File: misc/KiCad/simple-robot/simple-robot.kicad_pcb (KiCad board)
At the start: 4 copper layers, 100 x 100 mm, 69 parts, among them J1 MotLA, J10 Screw_Terminal_2_P5.00mm, J11 JSTHCSR04, J12 IR_RF, J13 IR_LF, J14 GV, J15 JST RF-LOG, J16 RF_PWR, J2 MotLB, J3 Servo, J4 MotRA, J5 MotRB, J6 ENC_LF, J7 ENC_LR, J8 ENC_RF, J9 ENC_RR, P1 Port Expander, SW1 RotaryEncoder_Switch, U1 Pico2, U2 CD4049UB

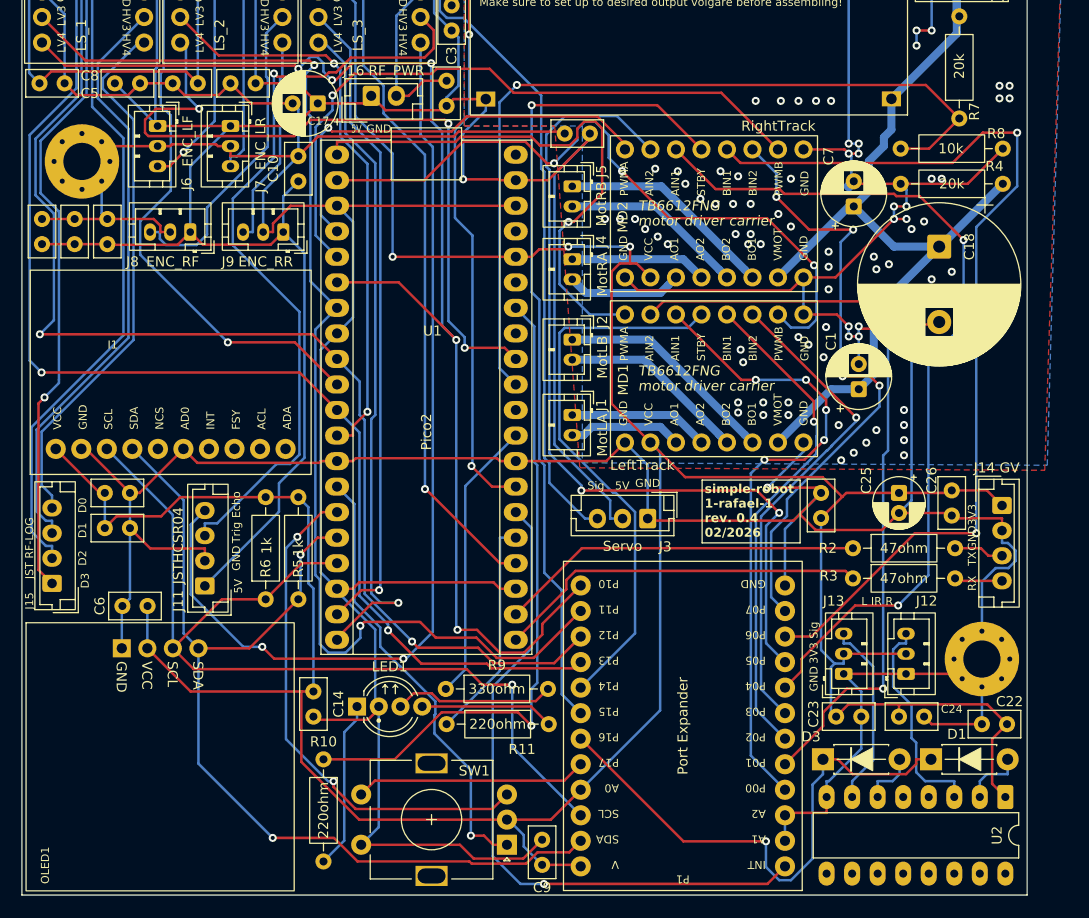
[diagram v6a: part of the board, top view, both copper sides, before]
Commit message: rp235x E9 erratum hitting: rotary encoder should be reffed to common GND instead of 3V3
Pulldowns on RP235x only work on after stepping A4, all my boards are
stepping A2. So thereference for the encoder should not be 3V3 because
that we will need to pull down and that will latch on the RP.

Workaround is to add pulldowns which i will do for now but a proper
workaround is to change the pcb and schematic to have a common GND
instead of common 3V3 on the encoder and use pullup.

This commit changes schematic and pcb.
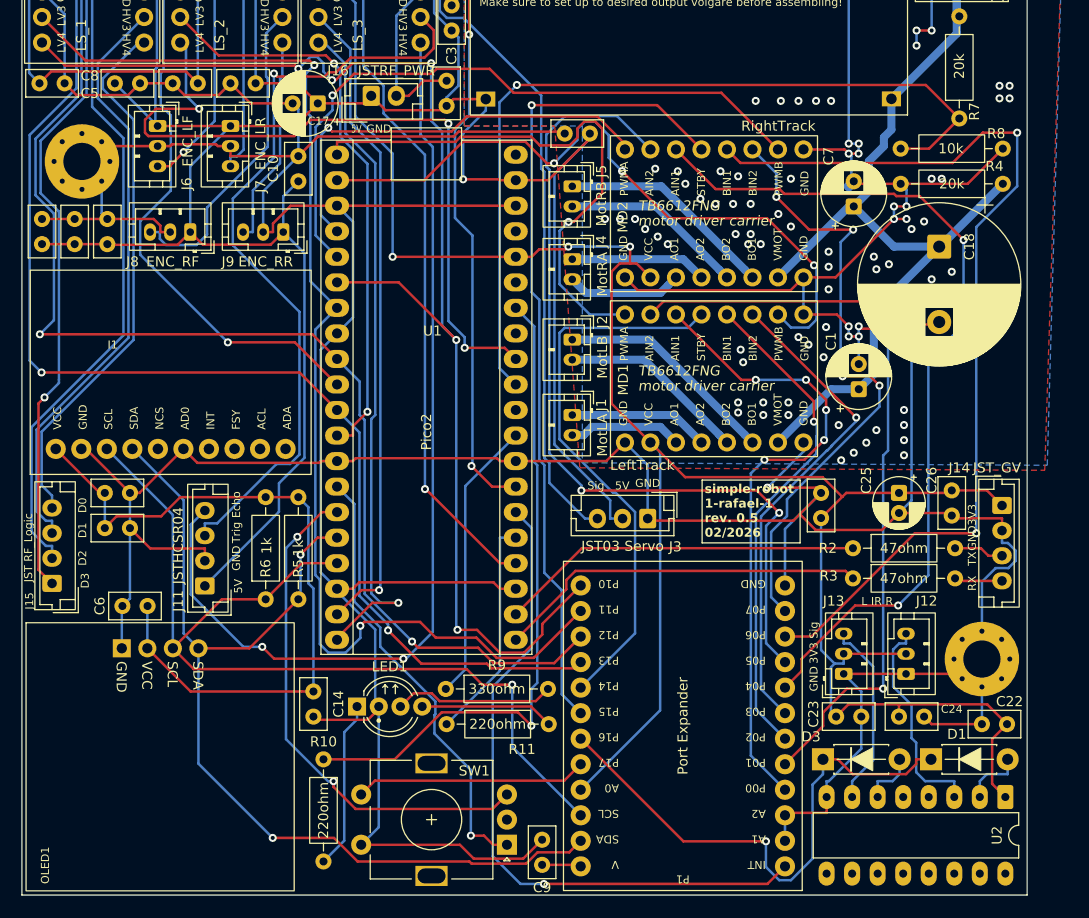
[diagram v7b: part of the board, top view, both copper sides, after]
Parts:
- J14: value GV -> JST_GV
- J15: value JST RF-LOG -> JST RF_Logic
- J16: value RF_PWR -> JSTRF_PWR
- J3: value Servo -> JST03 Servo
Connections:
- SW1 pad C: +3V3 -> GND
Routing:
- net +3V3: track 400.4 -> 355.9 mm
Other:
- board text added: "simple-robot 1-rafael-1 rev. 0.5 02/2026"
- board text removed: "simple-robot 1-rafael-1 rev. 0.4 02/2026"
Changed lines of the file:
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@@
 			)
 		)
-		(property "Value" "JST RF-LOG"
-			(at 3.5 -2.25 90)
+		(property "Value" "JST RF_Logic"
+			(at 3.55 -2.35 90)
 			(layer "F.SilkS")
 			(effects
@@
 		(tags "connector JST EH vertical")
 		(property "Reference" "J16"
-			(at -1.75 -2.5 0)
+			(at -3.3 -2.5 0)
 			(layer "F.SilkS")
 			(effects
@@
 			)
 		)
-		(property "Value" "RF_PWR"
+		(property "Value" "JSTRF_PWR"
 			(at 2.5 -2.5 0)
 			(layer "F.SilkS")
@@
 		(tags "connector JST EH vertical")
 		(property "Reference" "J14"
-			(at -3.75 1.75 0)
+			(at -3.75 4.25 0)
 			(layer "F.SilkS")
 			(effects
@@
 			)
 		)
-		(property "Value" "GV"
-			(at -3.75 -0.75 0)
+		(property "Value" "JST_GV"
+			(at -3.75 0.5 0)
 			(layer "F.SilkS")
 			(effects
@@
 			(layers "*.Cu" "*.Mask")
 			(remove_unused_layers no)
-			(net 3 "+3V3")
+			(net 9 "GND")
 			(pinfunction "C")
 			(pintype "passive")
@@
 		(tags "connector JST EH vertical")
 		(property "Reference" "J3"
-			(at -1.75 -2.8 0)
+			(at -2.75 -2.8 0)
 			(layer "F.SilkS")
 			(effects
@@
 			)
 		)
-		(property "Value" "Servo"
+		(property "Value" "JST03 Servo"
 			(at 2.5 -2.75 0)
 			(layer "F.SilkS")
@@
 		)
 	)
-	(gr_text "simple-robot\n1-rafael-1\nrev. 0.4\n02/2026"
+	(gr_text "simple-robot\n1-rafael-1\nrev. 0.5\n02/2026"
 		(at 122.667393 103.219377 0)
 		(layer "F.SilkS")
@@
 	)
 	(segment
-		(start 110.34 128.2775)
-		(end 107.3675 131.25)
-		(width 0.25)
-		(layer "F.Cu")
-		(net 3)
-	)
-	(segment
 		(start 106.2075 74.5117)
 		(end 108.849025 74.5117)
@@
 	)
 	(segment
-		(start 88.2962 131.25)
-		(end 103 131.25)
-		(width 0.25)
-		(layer "F.Cu")
-		(net 3)
-	)
-	(segment
 		(start 106.5 135.75)
 		(end 110.1925 135.75)
@@
 	)
 	(segment
-		(start 107.3675 131.25)
-		(end 103 131.25)
-		(width 0.25)
-		(layer "F.Cu")
-		(net 3)
-	)
-	(segment
 		(start 117.2771 77.31)
 		(end 115.9021 75.935)
@@
 	)
 	(segment
-		(start 82.5519 125.5057)
-		(end 88.2962 131.25)
-		(width 0.25)
-		(layer "F.Cu")
-		(net 3)
-	)
-	(segment
-		(start 82.5519 118.5)
-		(end 82.5519 125.5057)
-		(width 0.25)
-		(layer "F.Cu")
-		(net 3)
-	)
-	(segment
 		(start 150.75 98.5)
 		(end 152.25 100)
@@
 	)
 	(segment
-		(start 103.1371 131.25)
-		(end 103 131.25)
-		(width 0.25)
-		(layer "B.Cu")
-		(net 3)
-	)
-	(segment
 		(start 67.23 110.02)
 		(end 67.23 114.205)
@@
 	)
 	(segment
-		(start 104.6731 132.786)
-		(end 103.1371 131.25)
-		(width 0.25)
-		(layer "B.Cu")
-		(net 3)
-	)
-	(segment
 		(start 55.4733 56.9733)
 		(end 56.5 58)
@@
 	)
 	(segment
-		(start 104.6731 133.9231)
-		(end 104.6731 132.786)
-		(width 0.25)
-		(layer "B.Cu")
-		(net 3)
-	)
-	(segment
 		(start 136.5 114.75)
 		(end 136.5 115.7267)
@@
 	)
 	(segment
-		(start 106.5 135.75)
-		(end 104.6731 133.9231)
-		(width 0.25)
-		(layer "B.Cu")
-		(net 3)
-	)
-	(segment
 		(start 80.1306 39.9624)
 		(end 72.1315 47.9615)
@@
 		(width 0.25)
 		(layer "B.Cu")
+		(net 9)
+	)
+	(segment
+		(start 103.1371 131.25)
+		(end 103 131.25)
+		(width 0.25)
+		(layer "B.Cu")

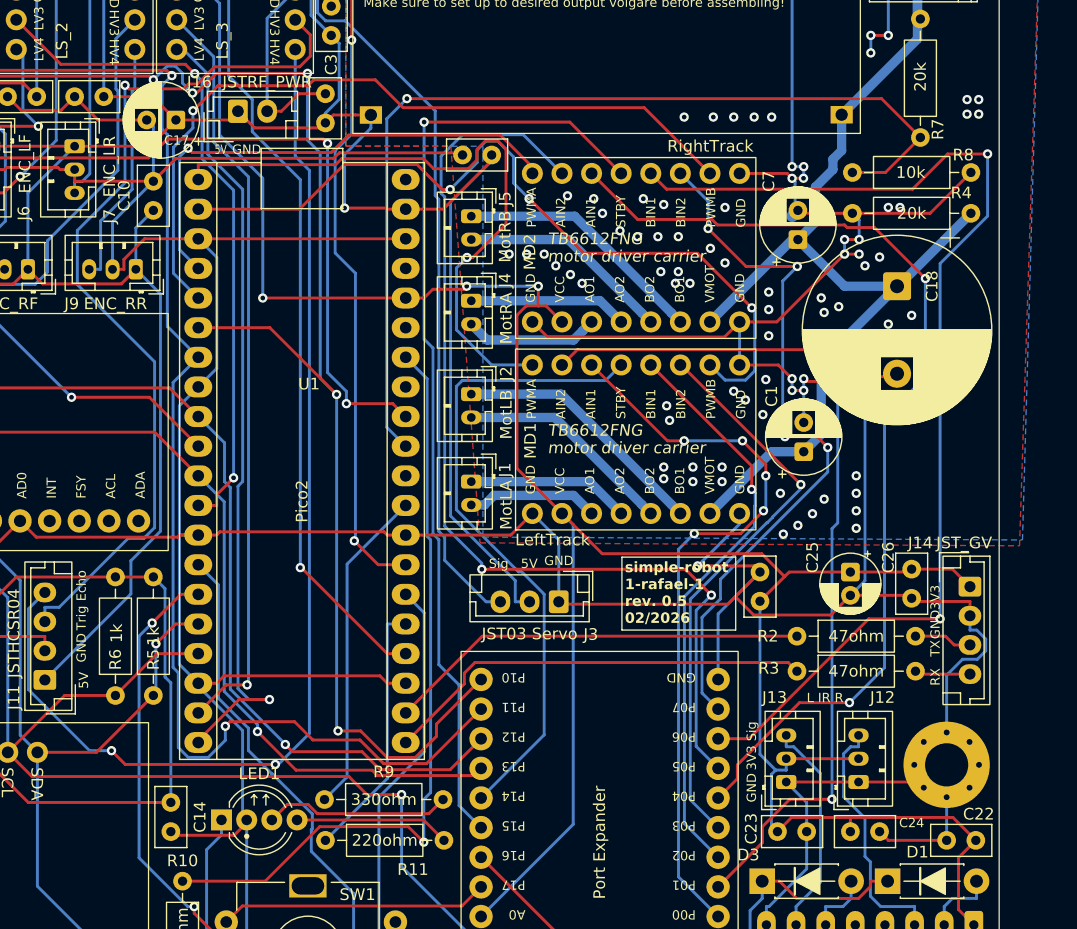
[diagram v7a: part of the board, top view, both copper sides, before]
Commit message: Ir us testmode (#33)
* new testmode for ultrasonic and ir sensors

* misassigned trig and echo pins fixed

* obstacle detection should blink the indicator

* Update schematic and pcb: IR_OBST net needs to be pulled low

* add ultrasonic sweep test mode

* The US measurements must not assume maximum distance if timing or
erroring out, in that case we simply have no data which represents cases
better, where we measure >maxdistance

* break test mode into more files, no blanket spawning of all test modes

* do not use us measurement >200cm

* dislay ownership conflict

* guard against running two testmode tasks simultaneously

* do not leak us values into later uses

* indicate obstacve and no obstacle

* clearer naming for test modes

* sweep was ONE line too long

* fmt

* review
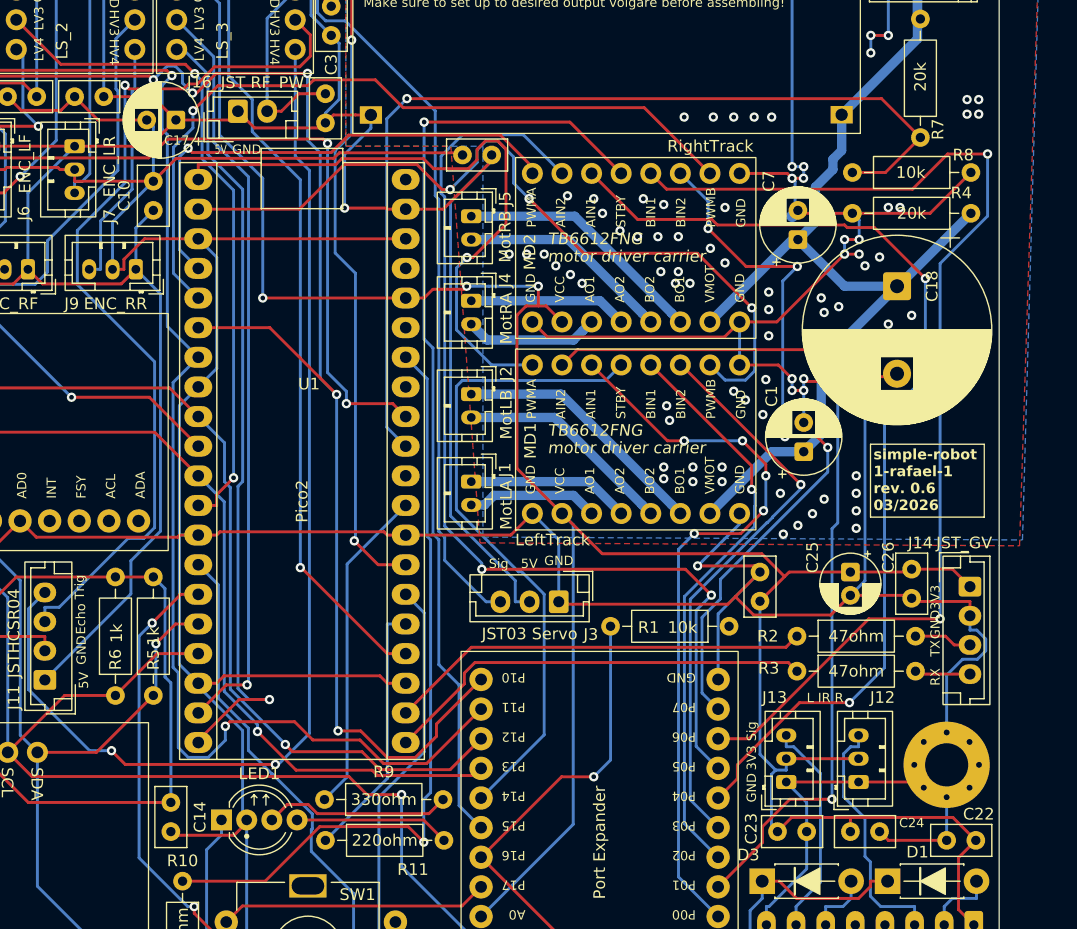
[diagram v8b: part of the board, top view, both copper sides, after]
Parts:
- added R1: 10k, Resistor_THT:R_Axial_DIN0207_L6.3mm_D2.5mm_P10.16mm_Horizontal, F.Cu at (131.6, 103.4)
- J16: value JSTRF_PWR -> JST RF_PW
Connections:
- U1 pad 19: US_ECHO -> US_TRIG
- U1 pad 20: US_TRIG -> US_ECHO
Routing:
- net IR_OBST: track 53.8 -> 79.8 mm, vias 1 -> 2
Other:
- board text added: "simple-robot 1-rafael-1 rev. 0.6 03/2026"
- board text removed: "simple-robot 1-rafael-1 rev. 0.5 02/2026"
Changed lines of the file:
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@@
 			)
 		)
-		(property "Value" "JSTRF_PWR"
-			(at 2.5 -2.5 0)
+		(property "Value" "JST RF_PW"
+			(at 2.1 -2.45 0)
 			(layer "F.SilkS")
 			(effects
@@
 			(layers "*.Cu" "*.Mask")
 			(remove_unused_layers no)
-			(net 28 "US_ECHO")
+			(net 30 "US_TRIG")
 			(pinfunction "GPIO14")
 			(pintype "bidirectional")
@@
 			(layers "*.Cu" "*.Mask")
 			(remove_unused_layers no)
-			(net 30 "US_TRIG")
+			(net 28 "US_ECHO")
 			(pinfunction "GPIO15")
 			(pintype "bidirectional")
@@
 		)
 	)
+	(footprint "Resistor_THT:R_Axial_DIN0207_L6.3mm_D2.5mm_P10.16mm_Horizontal"
+		(layer "F.Cu")
+		(at 131.6 103.4 180)
+		(descr "Resistor, Axial_DIN0207 series, Axial, Horizontal, pin pitch=10.16mm, 0.25W = 1/4W, length*diameter=6.3*2.5mm^2, http://cdn-reichelt.de/documents/datenblatt/B400/1_4W%23YAG.pdf")
+		(tags "Resistor Axial_DIN0207 series Axial Horizontal pin pitch 10.16mm 0.25W = 1/4W length 6.3mm diameter 2.5mm")
+		(property "Reference" "R1"
+			(at 6.9 -0.1 0)
+			(layer "F.SilkS")
+			(effects
+				(font
+					(size 1 1)
+					(thickness 0.15)
+				)
+			)
+		)
+		(property "Value" "10k"
+			(at 4 -0.1 0)
+			(layer "F.SilkS")
+			(effects
+				(font
+					(size 1 1)
+					(thickness 0.15)
+				)
+			)
+		)
+		(property "Datasheet" ""
+			(at 0 0 0)
+			(layer "F.Fab")
+			(hide yes)
+			(effects
+				(font
+					(size 1.27 1.27)
+					(thickness 0.15)
+				)
+			)
+		)
+		(property "Description" "10kΩ, 1/4W Resistor"
+			(at 0 0 0)
+			(layer "F.Fab")
+			(hide yes)
+			(effects
+				(font
+					(size 1.27 1.27)
+					(thickness 0.15)
+				)
+			)
+		)
+		(property ki_fp_filters "Resistor_THT:R_Axial_DIN0207_L6.3mm_D2.5mm*")
+		(sheetname "/")
+		(sheetfile "simple-robot.kicad_sch")
+		(attr through_hole)
+		(fp_line
+			(start 9.12 0)
+			(end 8.35 0)
+			(stroke
+				(width 0.12)
+				(type solid)
+			)
+			(layer "F.SilkS")
+		)
+		(fp_line
+			(start 1.04 0)
+			(end 1.81 0)
+			(stroke
+				(width 0.12)
+				(type solid)
+			)
+			(layer "F.SilkS")
+		)
+		(fp_rect
+			(start 1.81 -1.37)
+			(end 8.35 1.37)
+			(stroke
+				(width 0.12)
+				(type solid)
+			)
+			(fill no)
+			(layer "F.SilkS")
+		)
+		(fp_rect
+			(start -1.05 -1.5)
+			(end 11.21 1.5)
+			(stroke
+				(width 0.05)
+				(type solid)
+			)
+			(fill no)
+			(layer "F.CrtYd")
+		)
+		(fp_line
+			(start 10.16 0)
+			(end 8.23 0)
+			(stroke
+				(width 0.1)
+				(type solid)
+			)
+			(layer "F.Fab")
+		)
+		(fp_line
+			(start 0 0)
+			(end 1.93 0)
+			(stroke
+				(width 0.1)
+				(type solid)
+			)
+			(layer "F.Fab")
+		)
+		(fp_rect
+			(start 1.93 -1.25)
+			(end 8.23 1.25)
+			(stroke
+				(width 0.1)
+				(type solid)
+			)
+			(fill no)
+			(layer "F.Fab")
+		)
+		(fp_text user "${REFERENCE}"
+			(at 5.08 0 0)
+			(layer "F.Fab")
+			(effects
+				(font
+					(size 1 1)
+					(thickness 0.15)
+				)
+			)
+		)
+		(pad "1" thru_hole circle
+			(at 0 0 180)
+			(size 1.6 1.6)
+			(drill 0.8)
+			(layers "*.Cu" "*.Mask")
+			(remove_unused_layers no)
+			(net 9 "GND")
+			(pintype "passive")
+		)
+		(pad "2" thru_hole circle
+			(at 10.16 0 180)
+			(size 1.6 1.6)
+			(drill 0.8)
+			(layers "*.Cu" "*.Mask")
+			(remove_unused_layers no)
+			(net 34 "IR_OBST")
+			(pintype "passive")
+		)
+		(embedded_fonts no)
+		(model "${KICAD9_3DMODEL_DIR}/Resistor_THT.3dshapes/R_Axial_DIN0207_L6.3mm_D2.5mm_P10.16mm_Horizontal.step"
+			(offset
+				(xyz 0 0 0)
+			)
+			(scale
+				(xyz 1 1 1)
+			)
+			(rotate
+				(xyz 0 0 0)
+			)
+		)
+	)
 	(footprint "common-hobby-things:Level shifter 4 bi-dir"
 		(layer "F.Cu")
@@
 	)
 	(gr_rect
-		(start 122.417393 97.469377)
-		(end 132.167393 103.719377)
+		(start 143.724212 87.794158)
+		(end 153.474212 94.044158)
 		(stroke
 			(width 0.1)
@@
 	)
 	(gr_text "GND"
-		(at 76.55 106.5 90)
+		(at 76.55 106.7 90)
 		(layer "F.SilkS")
 		(effects
@@
 	)
 	(gr_text "Echo"
-		(at 76.55 101.25 90)
+		(at 76.5 104.1 90)
 		(layer "F.SilkS")
 		(effects
@@
 	)
 	(gr_text "Trig"
-		(at 76.55 103.75 90)
+		(at 76.4 101.1 90)
 		(layer "F.SilkS")
 		(effects
@@
 		)
 	)
-	(gr_text "simple-robot\n1-rafael-1\nrev. 0.5\n02/2026"
-		(at 122.667393 103.219377 0)
+	(gr_text "simple-robot\n1-rafael-1\nrev. 0.6\n03/2026"
+		(at 143.974212 93.544158 0)
 		(layer "F.SilkS")
 		(effects
@@
 	)
 	(segment
+		(start 117.2375 116.3)
+		(end 110.34 123.1975)
+		(width 0.25)
+		(layer "F.Cu")
+		(net 34)
+	)
+	(segment
 		(start 145.19 125.25)
 		(end 143.7133 125.25)
@@
 	)
 	(segment
+		(start 120 116.3)
+		(end 117.2375 116.3)
+		(width 0.25)
+		(layer "F.Cu")
+		(net 34)
+	)
+	(segment
 		(start 143.7133 125.7115)
 		(end 142.6981 126.7267)
@@
 		(net 34)
 	)
+	(via
+		(at 120 116.3)
+		(size 0.8)
+		(drill 0.4)
+		(layers "F.Cu" "B.Cu")
+		(net 34)
+	)
 	(via blind
 		(at 128.7671 133.4068)
@@
 	)
 	(segment
+		(start 121.44 103.4)
+		(end 121.44 114.86)
+		(width 0.25)
+		(layer "B.Cu")
+		(net 34)
+	)
+	(segment
 		(start 128.7671 135.9562)
 		(end 130.0851 137.2742)
@@
 	)
 	(segment
+		(start 121.44 114.86)
+		(end 120 116.3)
+		(width 0.25)
+		(layer "B.Cu")
+		(net 34)
+	)
+	(segment
 		(start 127.4257 81)
 		(end 127.5 81)
@@
 	)
 	(segment
-		(start 110.4525 104.25)
-		(end 103.88 110.8225)
+		(start 137.42 104.25)
+		(end 136.47 105.2)
 		(width 0.25)
 		(layer "F.Cu")
@@
 	)
 	(segment
-		(start 137.42 104.25)
-		(end 110.4525 104.25)
+		(start 136.47 105.2)
+		(end 109.5025 105.2)
+		(width 0.25)
+		(layer "F.Cu")
+		(net 83)
+	)
+	(segment
+		(start 109.5025 105.2)
+		(end 103.88 110.8225)
 		(width 0.25)
 		(layer "F.Cu")
